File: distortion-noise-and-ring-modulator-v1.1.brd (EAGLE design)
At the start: 44.8 x 24.1 mm, 75 parts, among them IC1 TL074JT, IC4 LM13700SL, IC5 TL074JT, Q1 MMBT3906, T1 NOISE-2N3904, U1 MC1496DR2G, X2 MA06-1JN, X3 MA06-1JN

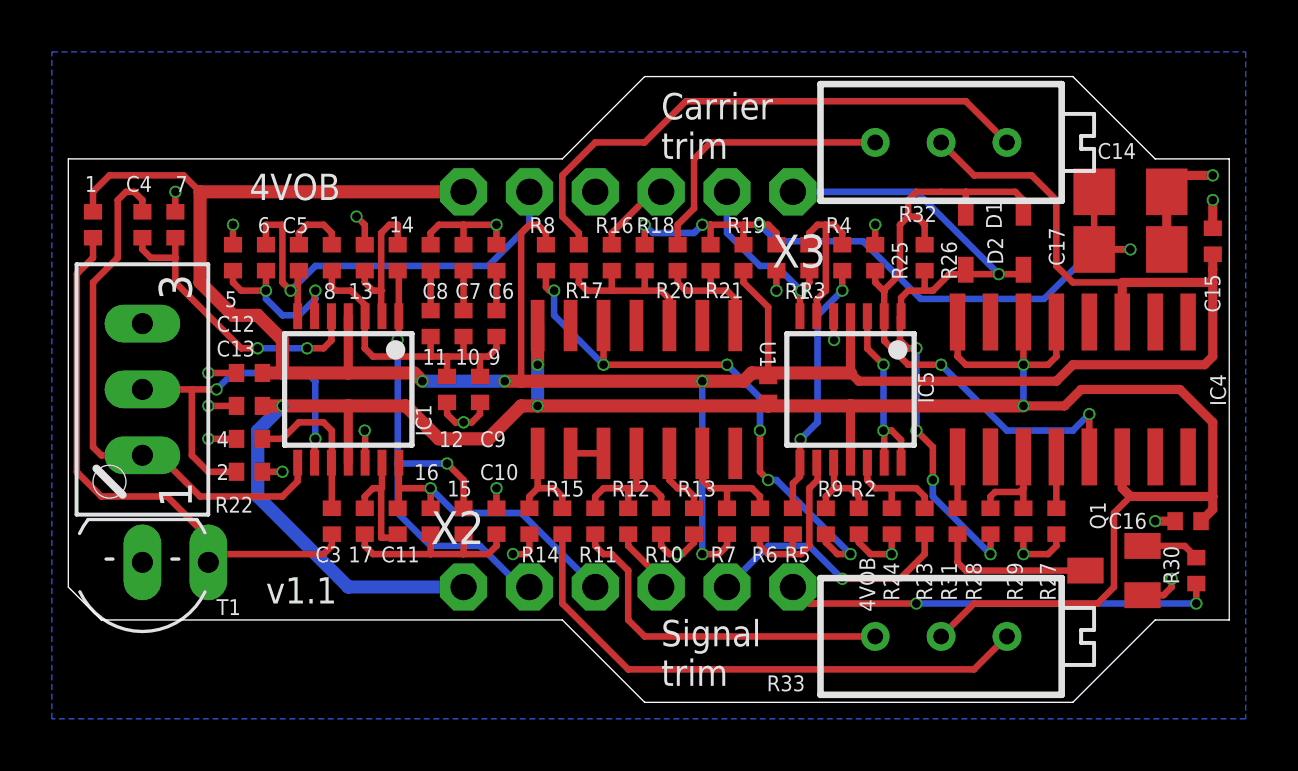
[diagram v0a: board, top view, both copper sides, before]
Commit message: Tested with JLCPCB
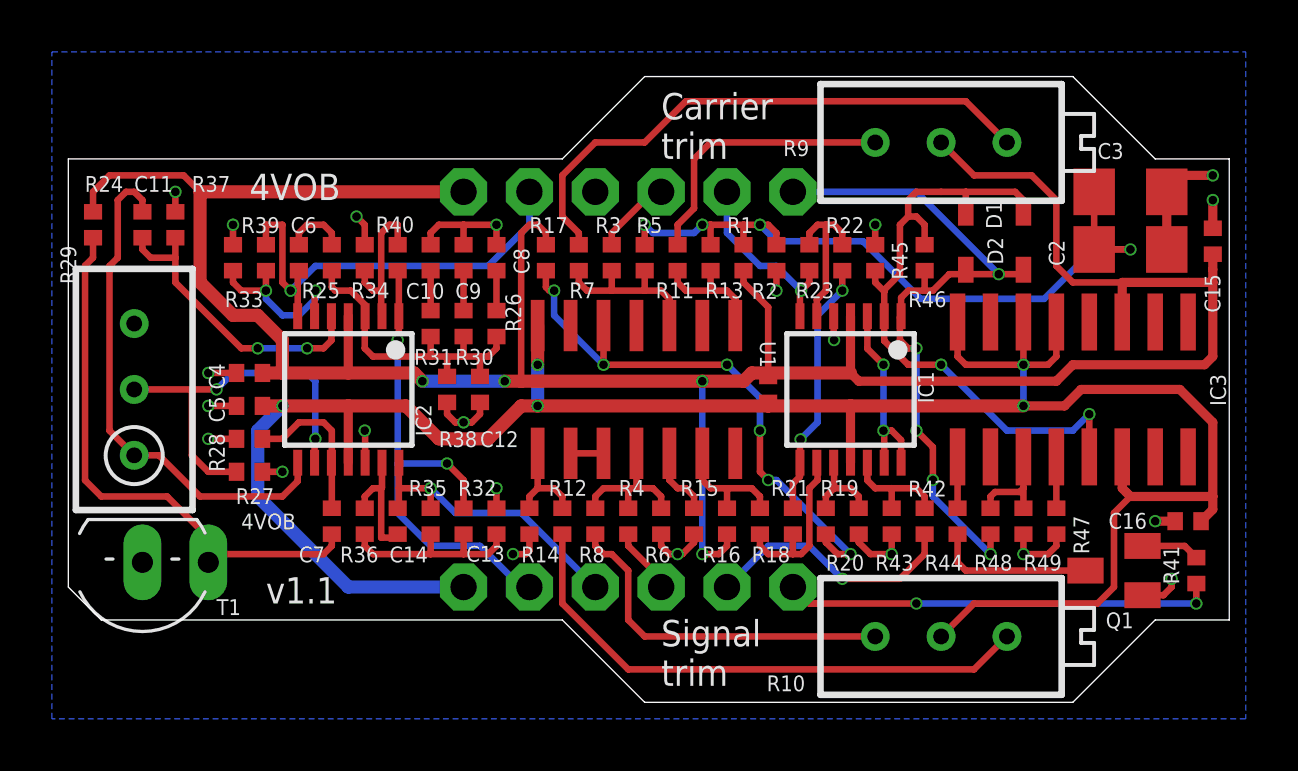
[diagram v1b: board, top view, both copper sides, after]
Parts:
- removed 1: 220k, rcl:R0402
- removed 10: 10k, rcl:R0402
- removed 11: 3k3, rcl:R0402
- removed 15: 4k7, rcl:R0402
- removed 2, 5: 1k, rcl:R0402
- removed 4: 100k, rcl:R0402
- removed 8: 68k, rcl:R0402
- removed 9: 33k, rcl:R0402
- removed C17: 47uF, rcl:C1206
- removed IC5: TL074JT, joakim:TSSOP14J
- removed X3: MA06-1JN, joakim:MA06N-1J
- added C1: 100n, joakim:C0402-J
- added IC2: TL074JT, joakim:TSSOP14J
- added R41: 8k2, rcl:R0402
- added R42, R46: 33k, rcl:R0402
- added R43, R45: 1k, rcl:R0402
- added R44: 10k, rcl:R0402
- added R47, R49: 510R, rcl:R0402
- added R48: 15k, rcl:R0402
- added X1: MA06-1JN, joakim:MA06N-1J
- C10: value 220n -> 10n
- C11: value 2n2 -> 470n
- C12: value 100nF -> 3n3
- C13: value 100nF -> 220n
- C14: value 47uF -> 2n2; device rcl:C1206 -> joakim:C0402-J
- C2: value 100n -> 47uF; device joakim:C0402-J -> rcl:C1206
- C3: value 470n -> 47uF; device joakim:C0402-J -> rcl:C1206
- C4, C5: value 470n -> 100nF
- C6: value 100n -> 470n
- C7: value 22n -> 470n
- C8: value 10n -> 100n
- C9: value 3n3 -> 22n
- R10: value 2k7 -> 500R; device rcl:R0402 -> rcl:RTRIM3296X
- R11: value 6k8 -> 12k
- R12: value 180k -> 6k8
- R13: value 6k8 -> 2k7
- R16: value 180k -> 1k2
- R17: value 12k -> 1k2
- R18, R21: value 2k7 -> 15k
- R19: value 1k5 -> 15k
- R2: value 15k -> 1k5
- R20: value 12k -> 15k
- R22: value 200k -> 10k; device pot:S64W -> rcl:R0402
- R23: value 33k -> 68k
- R24: value 1k -> 220k
- R25: value 1k -> 68k
- R27: value 510R -> 1k
- R28: value 15k -> 100k
- R29: value 510R -> 200k; device rcl:R0402 -> rcl:RTRIM3296W
- R3: value 68k -> 180k
- R30: value 8k2 -> 10k
- R31: value 10k -> 3k3
- R32: value 500R -> 4k7; device rcl:RTRIM3296X -> rcl:R0402
- R33: value 500R -> 1k; device rcl:RTRIM3296X -> rcl:R0402
- R4: value 10k -> 180k
- R5, R6: value 15k -> 2k7
- R7: value 1k2 -> 12k
- R8: value 1k2 -> 6k8
- R9: value 15k -> 500R; device rcl:R0402 -> rcl:RTRIM3296X
- moved R29 34.7 mm to (2.54, 11.4), turned to 0 degrees
- moved C3 33.3 mm to (41.0, 19.1), turned to 0 degrees
- moved R24 32.9 mm to (0.95, 17.8), turned to 90 degrees
- moved R27 31.2 mm to (6.99, 8.26), turned to 0 degrees
- moved C14 31.0 mm to (12.7, 6.35), turned to 270 degrees
- moved R33 31.0 mm to (6.35, 16.5)
- moved R30 29.8 mm to (15.2, 14.0), turned to 90 degrees
- moved R28 28.8 mm to (6.99, 9.53), turned to 180 degrees
- moved R22 28.7 mm to (29.8, 16.5), turned to 90 degrees
- moved R32 23.5 mm to (15.2, 6.35)
- moved R31 21.7 mm to (14.0, 14.0), turned to 90 degrees
- moved R25 21.0 mm to (10.2, 16.5), turned to 90 degrees
- moved IC1 19.4 mm to (30.2, 11.4)
- moved R26 16.7 mm to (16.5, 14.0), turned to 90 degrees
- moved R9 15.3 mm to (33.7, 21.0)
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- renumbered 12 to R38, 13 to R34, 14 to R40, 16 to R35, 17 to R36, 6 to R39, 7 to R37, IC4 to IC3
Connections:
- net +12V: now also C1.2, C4.2, IC2.4, R1.2, R16.2, R17.1, R24.2, R9.2, X2.6; no longer 1.2, C12.2, C2.2, IC5.4, R19.2, R32.2, R7.2, R8.1, X3.6
- net -12V: now also C1.1, C5.1, IC2.11, R10.2, X1.1; no longer C13.1, C2.1, IC5.11, R33.2, X2.1
- net CARRIER: now also R3.1, X2.3; no longer R16.1, X3.3
- net CARRIER_IN: now also R3.2, R5.1, R7.1; no longer R16.2, R17.1, R18.1
- net CAR_TRIM_1: now also R7.2, R9.3; no longer R17.2, R32.3
- net CAR_TRIM_2: now also R11.2, R9.1; no longer R20.2, R32.1
- net COUT1: now also R17.2, R19.2; no longer R8.2, R9.2
- net COUT2: now also R16.1, R18.2; no longer R6.2, R7.1
- net DIST_CV: now also R41.2, X1.6; no longer R30.2, X2.6
- net DIST_IN: now also R42.1, X1.5; no longer R23.1, X2.5
- net DIST_I_ABC: now also R44.1; no longer R31.1
- net DIST_OUT: now also IC1.1, R46.2, R48.1, X2.1; no longer IC5.1, R26.2, R28.1, X3.1
- net GND: now also C13.1, C2.2, C3.2, C4.1, C5.2, IC1.5, IC2.12, R15.1, R2.1, R20.2, R27.2, R28.2, R33.1, R43.2, R45.1, R47.1, R49.1, R6.1, X2.4; no longer 2.2, 4.2, 5.1, C13.2, C14.2, C17.2, C6.1, C7.1, IC1.12, IC5.5, R1.1, R10.1, R13.1, R2.2, R24.2, R25.1, R27.1, R29.1, X3.4
- net LEV1: now also IC2.9, R27.1, R29.2; no longer 2.1, IC1.9, R22.S
- net LEV2: now also C11.1, IC2.8, R29.1; no longer C4.1, IC1.8, R22.A
- net N$1: now also IC2.2; no longer IC1.2
- net N$10: now also C7.2, IC2.10, R28.1; no longer 4.1, C3.2, IC1.10
- net N$11: now also R15.2; no longer R13.2
- net N$13: now also C11.2, IC2.5; no longer C4.2, IC1.5
- net N$14: now also C12.2, IC2.3, R25.1, R26.1, R30.1, R31.1; no longer 10.1, 11.1, 8.1, 9.1, C9.2, IC1.3
- net N$15: now also IC1.10, R19.1, R20.1; no longer IC5.10, R2.1, R9.1
- net N$16: now also IC1.9, R18.1, R21.1; no longer IC5.9, R5.1, R6.1
- net N$17: now also IC1.8, R21.2, R22.1; no longer IC5.8, R4.1, R5.2
- net N$18: now also IC1.6, R22.2, R23.1; no longer IC5.6, R3.1, R4.2
- net N$19: now also C6.2, R25.2; no longer 8.2, C5.2
- net N$2: now also IC2.6, R33.2; no longer 5.2, IC1.6
- net N$20: now also C13.2, R32.2; no longer 15.2, C10.2
- net N$21: now also C14.2, IC2.13; no longer C11.2, IC1.13
- net N$22: now also IC1.12, R42.2, R43.1; no longer IC5.12, R23.2, R24.1
- net N$23: now also IC1.13, IC1.14, IC1.3; no longer IC5.13, IC5.14, IC5.3
- net N$24: now also IC1.2, R45.2, R46.1; no longer IC5.2, R25.2, R26.1
- net N$25: now also R47.2; no longer R27.2
- net N$26: now also R48.2, R49.2; no longer R28.2, R29.2
- net N$27: now also R41.1; no longer R30.1
- net N$28: now also R44.2; no longer R31.2
- net N$3: now also R12.2; no longer R15.2
- net N$4: now also C8.2, R26.2; no longer 9.2, C6.2
- net N$5: now also C9.2, R30.2; no longer 10.2, C7.2
- net N$6: now also C10.2, R31.2; no longer 11.2, C8.2
- net N$7: now also C7.1, R24.1; no longer 1.1, C3.1
- net N$8: now also R11.1, R13.1; no longer R20.1, R21.1
- net N$9: now also C2.1, C3.1, R1.1, R13.2, R2.2, R5.2; no longer C14.1, C17.1, R1.2, R18.2, R19.1, R21.2
- net OUT: now also IC1.7, R23.2, X2.2; no longer IC5.7, R3.2, X3.2
- net PINK: now also IC2.1, R32.1, X1.2; no longer 15.1, IC1.1, X2.2
- net RED: now also C14.1, IC2.14, X1.3; no longer C11.1, IC1.14, X2.3
- net SIGNAL: now also R4.1, X1.4; no longer R12.1, X2.4
- net SIG_IN: now also R4.2, R6.2, R8.2; no longer R10.2, R11.2, R12.2
- net SIG_TRIM_1: now also R10.1, R8.1; no longer R11.1, R33.1
- net SIG_TRIM_2: now also R10.3, R12.1; no longer R15.1, R33.3
- net WHITE: now also C6.1, IC2.7, X2.5; no longer C5.1, IC1.7, X3.5
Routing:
- net LEV2: track 21.2 -> 20.0 mm

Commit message: Fixed 1uF caps
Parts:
- C1: value 100n -> 1uF
- C15, C16, C4, C5: value 100nF -> 1uF
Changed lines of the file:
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@@
 <attribute name="VALUE" x="26.035" y="5.715" size="1.27" layer="27" rot="R90"/>
 </element>
-<element name="C1" library="joakim" package="C0402-J" value="100n" x="26.9875" y="11.43" smashed="yes" rot="R90">
+<element name="C1" library="joakim" package="C0402-J" value="1uF" x="26.9875" y="11.43" smashed="yes" rot="R90">
 <attribute name="VALUE" x="29.2735" y="10.541" size="1.27" layer="27" rot="R90"/>
 </element>
@@
 <attribute name="VALUE" x="6.895" y="14.68" size="1.27" layer="27" rot="R270"/>
 </element>
-<element name="C4" library="joakim" package="C0402-J" value="100nF" x="6.985" y="12.065" smashed="yes">
+<element name="C4" library="joakim" package="C0402-J" value="1uF" x="6.985" y="12.065" smashed="yes">
 <attribute name="NAME" x="6.0325" y="11.43" size="0.6096" layer="25" font="vector" rot="R90"/>
 <attribute name="VALUE" x="6.35" y="10.16" size="1.27" layer="27"/>
@@
 <attribute name="VALUE" x="-2.2606" y="8.509" size="1.27" layer="27" ratio="10"/>
 </element>
-<element name="C5" library="joakim" package="C0402-J" value="100nF" x="6.985" y="10.795" smashed="yes" rot="R180">
+<element name="C5" library="joakim" package="C0402-J" value="1uF" x="6.985" y="10.795" smashed="yes" rot="R180">
 <attribute name="NAME" x="6.0325" y="10.16" size="0.6096" layer="25" font="vector" rot="R90"/>
 <attribute name="VALUE" x="7.62" y="12.7" size="1.27" layer="27" rot="R180"/>
@@
 <attribute name="VALUE" x="45.212" y="9.525" size="1.27" layer="27" rot="R90"/>
 </element>
-<element name="C15" library="joakim" package="C0402-J" value="100nF" x="44.1325" y="17.145" smashed="yes" rot="R90">
+<element name="C15" library="joakim" package="C0402-J" value="1uF" x="44.1325" y="17.145" smashed="yes" rot="R90">
 <attribute name="NAME" x="43.815" y="15.875" size="0.6096" layer="25" font="vector" rot="R270"/>
 <attribute name="VALUE" x="46.0375" y="16.51" size="1.27" layer="27" rot="R90"/>
 </element>
-<element name="C16" library="joakim" package="C0402-J" value="100nF" x="43.18" y="6.35" smashed="yes">
+<element name="C16" library="joakim" package="C0402-J" value="1uF" x="43.18" y="6.35" smashed="yes">
 <attribute name="NAME" x="41.5925" y="6.6675" size="0.6096" layer="25" font="vector" rot="R180"/>
 <attribute name="VALUE" x="42.545" y="4.445" size="1.27" layer="27"/>

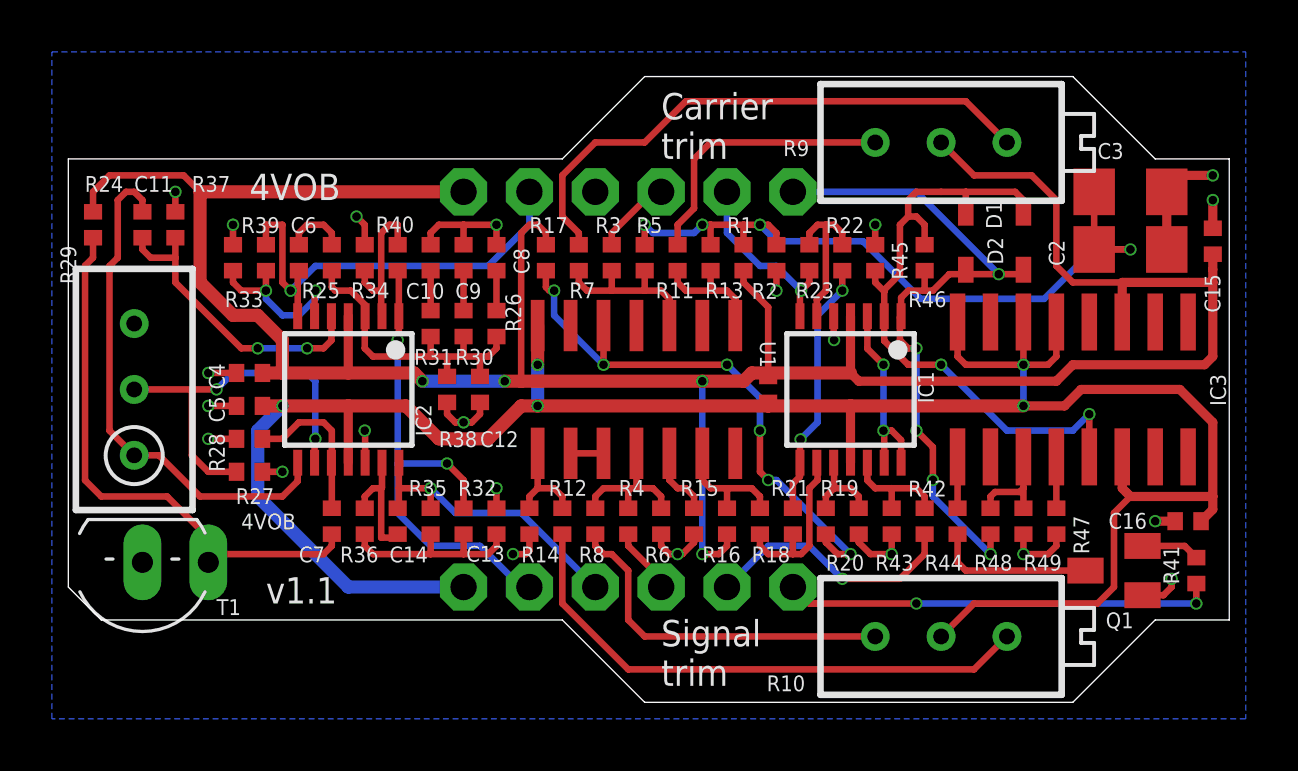
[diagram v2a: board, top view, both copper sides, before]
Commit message: Replaced several parts with 0603 to be able to use basic parts
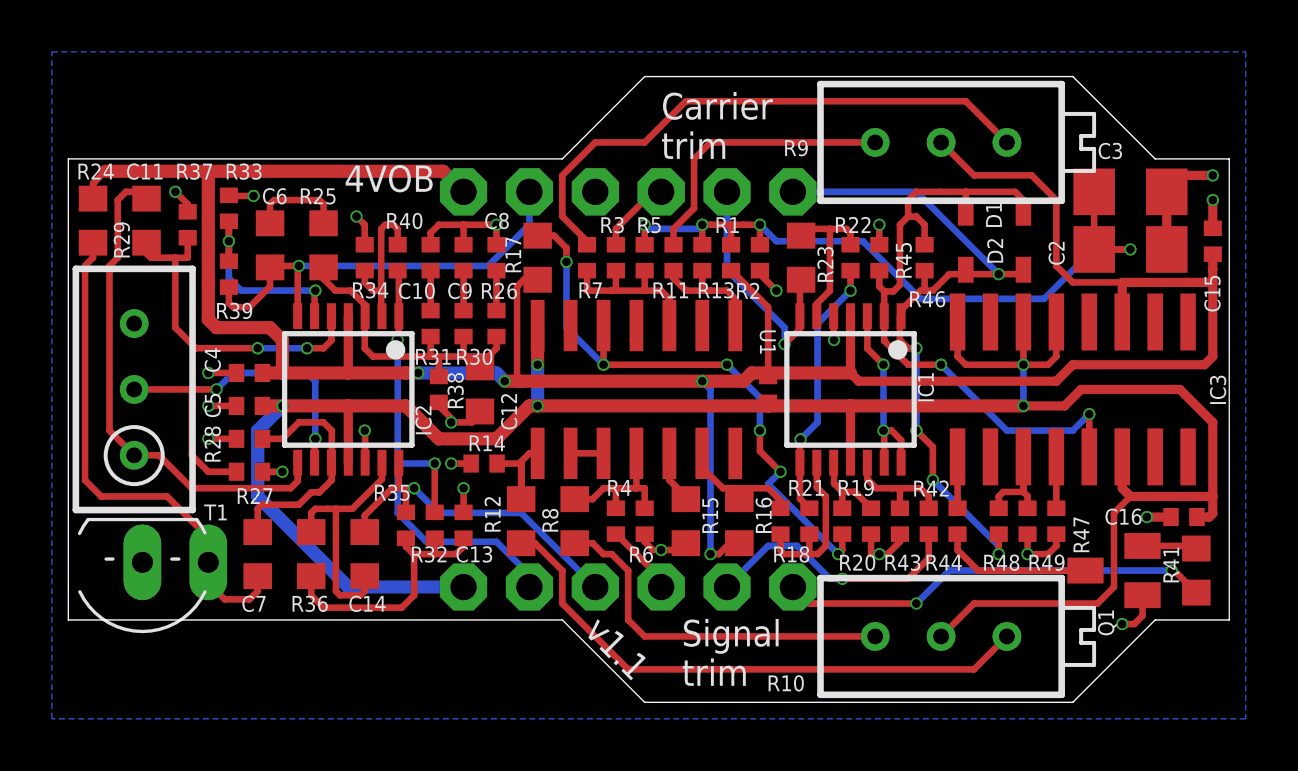
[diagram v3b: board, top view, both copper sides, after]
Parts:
- C11, C12, C14, C6, C7: device joakim:C0402-J -> joakim:C0603-J
- R12, R15, R16, R17, R23, R24, R25, R36, R41, R8: device rcl:R0402 -> rcl:R0603
- moved C7 3.13 mm to (7.30, 5.08)
- moved R14 2.83 mm to (16.0, 8.57), turned to 0 degrees
- moved R36 2.42 mm to (9.37, 5.08)
- moved R33 1.91 mm to (6.19, 18.4)
- moved C14 1.80 mm to (11.4, 5.08)
- moved R12 1.59 mm to (17.5, 6.35)
- moved R39 1.56 mm to (6.19, 15.9), turned to 270 degrees
- moved C13 1.28 mm to (15.2, 6.19)
- moved C6 1.21 mm to (7.78, 17.0)
- moved R32 1.12 mm to (14.1, 6.19)
- moved R35 0.97 mm to (13.0, 6.19)
- moved R18 0.79 mm to (27.5, 6.35)
- moved R8 0.79 mm to (19.5, 6.35)
- moved R19 0.63 mm to (29.8, 6.35)
- moved R2 0.63 mm to (26.7, 16.5)
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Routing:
- net N$21: track 4.81 -> 9.64 mm
- net N$10: track 6.07 -> 9.21 mm
- net OUT: track 7.27 -> 10.0 mm
- net N$20: track 7.79 -> 10.4 mm
- net RED: track 11.7 -> 13.8 mm
- net N$7: track 21.6 -> 19.6 mm
- net +12V: track 106.0 -> 104.4 mm
- net N$2: track 6.69 -> 8.27 mm
- net N$13: track 11.7 -> 12.9 mm
- net N$19: track 2.44 -> 3.67 mm
- net COUT1: track 21.8 -> 23.0 mm
- net COUT2: track 4.74 -> 5.51 mm
- net N$3: track 3.78 -> 4.52 mm
- net N$11: track 2.70 -> 2.03 mm
- net SIG_TRIM_2: track 21.4 -> 22.0 mm
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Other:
- outline, holes or cut-outs redrawn

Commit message: More basic parts
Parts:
- R13, R14, R5, R6: device rcl:R0402 -> rcl:R0603
- moved R8 8.90 mm to (27.1, 1.75), turned to 180 degrees
- moved R12 8.77 mm to (24.0, 0.48), turned to 180 degrees
- moved R7 4.78 mm to (21.7, 21.0), turned to 0 degrees
- moved R14 2.93 mm to (17.9, 6.35), turned to 90 degrees
- moved R6 1.59 mm to (20.6, 6.35), turned to 270 degrees
- moved R5 1.43 mm to (20.8, 16.5)
- moved R3 1.27 mm to (22.4, 16.5)
- moved R1 1.16 mm to (26.7, 16.2)
- moved R23 1.16 mm to (29.4, 16.8)
- moved R2 1.12 mm to (27.8, 16.7)
- moved R4 1.11 mm to (22.2, 6.35)
- moved R45 0.79 mm to (32.1, 16.5)
- moved R22 0.79 mm to (31.0, 16.5)
- moved R13 0.63 mm to (25.1, 16.5)
- moved D1 0.32 mm to (34.9, 17.1)
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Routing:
- net SIG_TRIM_1: track 14.2 -> 3.18 mm
- net SIG_TRIM_2: track 22.0 -> 12.0 mm
- net CARRIER_IN: track 6.65 -> 15.5 mm
- net N$3: track 4.52 -> 12.0 mm
- net SIG_IN: track 5.76 -> 13.1 mm
- net CAR_TRIM_1: track 22.1 -> 15.3 mm
- net N$18: track 6.11 -> 9.32 mm
- net N$9: track 27.5 -> 29.1 mm
- net N$24: track 25.7 -> 24.3 mm
- net OUT: track 10.0 -> 10.9 mm
- net +12V: track 104.4 -> 103.6 mm
- net GND: track 35.3 -> 35.6 mm, vias 22 -> 24
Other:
- board text added: "Signal"
- board text removed: "Signal trim"
